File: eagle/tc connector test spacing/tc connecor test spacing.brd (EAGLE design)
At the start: 100 x 52 mm, 31 parts

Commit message: Inside and outside draft versions chosen.
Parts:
- removed U$1, U$10, U$11, U$12, U$15, U$16, U$17, U$18, U$19, U$2, U$20, U$21, U$22, U$23, U$24, U$27, U$28, U$3, U$4, U$5, U$6, U$7, U$8, U$9: TC-MINI-SINGLE, PaxInstruments-Connectors:TC-CLIP-SINGLE
- removed U$29, U$30: POGO-2.54-2P, PaxInstruments-Connectors:POGO-2.54-2P
- removed U$31: POGO-2.54-6P, PaxInstruments-Connectors:POGO-2.54-6P
- moved U$25 43.9 mm to (12.0, 44.0)
- moved U$26 43.9 mm to (5.00, 44.0)
- moved U$13 37.0 mm to (5.00, 6.00)
- moved U$14 37.0 mm to (15.0, 6.00)
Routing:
- net N$1: track 27.0 -> 0.00 mm
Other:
- board size 100 x 52 mm -> 50 x 52 mm
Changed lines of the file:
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@@
 <board>
 <plain>
-<wire x1="0" y1="0" x2="100" y2="0" width="0.1" layer="20"/>
-<wire x1="100" y1="0" x2="100" y2="52" width="0.1" layer="20"/>
-<wire x1="100" y1="52" x2="0" y2="52" width="0.1" layer="20"/>
+<wire x1="0" y1="0" x2="50" y2="0" width="0.1" layer="20"/>
+<wire x1="50" y1="0" x2="50" y2="52" width="0.1" layer="20"/>
+<wire x1="50" y1="52" x2="0" y2="52" width="0.1" layer="20"/>
 <wire x1="0" y1="52" x2="0" y2="0" width="0.1" layer="20"/>
 <dimension x1="2" y1="-4" x2="13" y2="-4" x3="7.5" y3="-7" textsize="1.778" layer="48"/>
 <dimension x1="17" y1="-4" x2="22" y2="-4" x3="19.5" y3="-7" textsize="1.778" layer="48"/>
-<wire x1="3.5" y1="38" x2="14.5" y2="38" width="0.4064" layer="48"/>
 <wire x1="17" y1="-3" x2="22" y2="-3" width="0.4064" layer="48"/>
-<wire x1="22" y1="38" x2="33" y2="38" width="0.4064" layer="48"/>
-<wire x1="41.5" y1="38" x2="52.5" y2="38" width="0.4064" layer="48"/>
-<wire x1="62" y1="38" x2="73" y2="38" width="0.4064" layer="48"/>
-<wire x1="83.5" y1="38" x2="94.5" y2="38" width="0.4064" layer="48"/>
 <wire x1="2" y1="-3" x2="13" y2="-3" width="0.4064" layer="48"/>
-<wire x1="6.5" y1="14" x2="11.5" y2="14" width="0.4064" layer="48"/>
-<wire x1="25" y1="14" x2="30" y2="14" width="0.4064" layer="48"/>
-<wire x1="44.5" y1="14" x2="49.5" y2="14" width="0.4064" layer="48"/>
-<wire x1="65" y1="14" x2="70" y2="14" width="0.4064" layer="48"/>
-<wire x1="86.5" y1="14" x2="91.5" y2="14" width="0.4064" layer="48"/>
-<wire x1="31" y1="18" x2="26" y2="18" width="0.4064" layer="48"/>
-<wire x1="11" y1="18" x2="6" y2="18" width="0.4064" layer="48"/>
-<wire x1="43.5" y1="18" x2="54.5" y2="18" width="0.4064" layer="48"/>
-<wire x1="63" y1="18" x2="74" y2="18" width="0.4064" layer="48"/>
-<wire x1="2" y1="31" x2="16" y2="31" width="0.8" layer="46"/>
-<wire x1="18" y1="31" x2="39" y2="31" width="0.8" layer="46"/>
-<wire x1="41" y1="31" x2="56" y2="31" width="0.8" layer="46"/>
-<wire x1="58" y1="31" x2="79" y2="31" width="0.8" layer="46"/>
-<wire x1="81" y1="31" x2="98" y2="31" width="0.8" layer="46"/>
+<wire x1="7.5" y1="14" x2="12.5" y2="14" width="0.4064" layer="48"/>
+<wire x1="3.5" y1="36" x2="14.5" y2="36" width="0.4064" layer="48"/>
 <dimension x1="26" y1="-4" x2="43" y2="-4" x3="34.5" y3="-7" textsize="1.778" layer="48"/>
 <wire x1="26" y1="-3" x2="43" y2="-3" width="0.4064" layer="48"/>
@@
 </autorouter>
 <elements>
-<element name="U$1" library="PaxInstruments-Connectors" package="TC-CLIP-SINGLE" value="TC-MINI-SINGLE" x="23" y="46"/>
-<element name="U$2" library="PaxInstruments-Connectors" package="TC-CLIP-SINGLE" value="TC-MINI-SINGLE" x="32" y="46" rot="R180"/>
-<element name="U$3" library="PaxInstruments-Connectors" package="TC-CLIP-SINGLE" value="TC-MINI-SINGLE" x="13" y="46" rot="R180"/>
-<element name="U$4" library="PaxInstruments-Connectors" package="TC-CLIP-SINGLE" value="TC-MINI-SINGLE" x="5" y="46"/>
-<element name="U$5" library="PaxInstruments-Connectors" package="TC-CLIP-SINGLE" value="TC-MINI-SINGLE" x="42" y="46"/>
-<element name="U$6" library="PaxInstruments-Connectors" package="TC-CLIP-SINGLE" value="TC-MINI-SINGLE" x="52" y="46" rot="R180"/>
-<element name="U$7" library="PaxInstruments-Connectors" package="TC-CLIP-SINGLE" value="TC-MINI-SINGLE" x="62" y="46"/>
-<element name="U$8" library="PaxInstruments-Connectors" package="TC-CLIP-SINGLE" value="TC-MINI-SINGLE" x="73" y="46" rot="R180"/>
-<element name="U$9" library="PaxInstruments-Connectors" package="TC-CLIP-SINGLE" value="TC-MINI-SINGLE" x="5" y="6" rot="R180"/>
-<element name="U$10" library="PaxInstruments-Connectors" package="TC-CLIP-SINGLE" value="TC-MINI-SINGLE" x="13" y="6"/>
-<element name="U$11" library="PaxInstruments-Connectors" package="TC-CLIP-SINGLE" value="TC-MINI-SINGLE" x="23" y="6" rot="R180"/>
-<element name="U$12" library="PaxInstruments-Connectors" package="TC-CLIP-SINGLE" value="TC-MINI-SINGLE" x="32" y="6"/>
-<element name="U$13" library="PaxInstruments-Connectors" package="TC-CLIP-SINGLE" value="TC-MINI-SINGLE" x="42" y="6" rot="R180"/>
-<element name="U$14" library="PaxInstruments-Connectors" package="TC-CLIP-SINGLE" value="TC-MINI-SINGLE" x="52" y="6"/>
-<element name="U$15" library="PaxInstruments-Connectors" package="TC-CLIP-SINGLE" value="TC-MINI-SINGLE" x="73" y="6"/>
-<element name="U$16" library="PaxInstruments-Connectors" package="TC-CLIP-SINGLE" value="TC-MINI-SINGLE" x="95" y="46" rot="R180"/>
-<element name="U$17" library="PaxInstruments-Connectors" package="TC-CLIP-SINGLE" value="TC-MINI-SINGLE" x="62" y="6" rot="R180"/>
-<element name="U$18" library="PaxInstruments-Connectors" package="TC-CLIP-SINGLE" value="TC-MINI-SINGLE" x="83" y="46"/>
-<element name="U$19" library="PaxInstruments-Connectors" package="TC-CLIP-SINGLE" value="TC-MINI-SINGLE" x="22" y="26" rot="R180"/>
-<element name="U$20" library="PaxInstruments-Connectors" package="TC-CLIP-SINGLE" value="TC-MINI-SINGLE" x="12" y="26"/>
-<element name="U$21" library="PaxInstruments-Connectors" package="TC-CLIP-SINGLE" value="TC-MINI-SINGLE" x="83" y="6" rot="R180"/>
-<element name="U$22" library="PaxInstruments-Connectors" package="TC-CLIP-SINGLE" value="TC-MINI-SINGLE" x="95" y="6"/>
-<element name="U$23" library="PaxInstruments-Connectors" package="TC-CLIP-SINGLE" value="TC-MINI-SINGLE" x="35" y="26"/>
-<element name="U$24" library="PaxInstruments-Connectors" package="TC-CLIP-SINGLE" value="TC-MINI-SINGLE" x="5" y="26" rot="R180"/>
-<element name="U$25" library="PaxInstruments-Connectors" package="TC-CLIP-SINGLE" value="TC-MINI-SINGLE" x="52" y="26" rot="R180"/>
-<element name="U$26" library="PaxInstruments-Connectors" package="TC-CLIP-SINGLE" value="TC-MINI-SINGLE" x="45" y="26"/>
-<element name="U$27" library="PaxInstruments-Connectors" package="TC-CLIP-SINGLE" value="TC-MINI-SINGLE" x="62" y="26"/>
-<element name="U$28" library="PaxInstruments-Connectors" package="TC-CLIP-SINGLE" value="TC-MINI-SINGLE" x="75" y="26" rot="R180"/>
-<element name="U$29" library="PaxInstruments-Connectors" package="POGO-2.54-2P" value="POGO-2.54-2P" x="83" y="28"/>
-<element name="U$30" library="PaxInstruments-Connectors" package="POGO-2.54-2P" value="POGO-2.54-2P" x="93" y="28"/>
-<element name="U$31" library="PaxInstruments-Connectors" package="POGO-2.54-6P" value="POGO-2.54-6P" x="83" y="21"/>
+<element name="U$13" library="PaxInstruments-Connectors" package="TC-CLIP-SINGLE" value="TC-MINI-SINGLE" x="5" y="6" rot="R180"/>
+<element name="U$14" library="PaxInstruments-Connectors" package="TC-CLIP-SINGLE" value="TC-MINI-SINGLE" x="15" y="6"/>
+<element name="U$25" library="PaxInstruments-Connectors" package="TC-CLIP-SINGLE" value="TC-MINI-SINGLE" x="12" y="44" rot="R180"/>
+<element name="U$26" library="PaxInstruments-Connectors" package="TC-CLIP-SINGLE" value="TC-MINI-SINGLE" x="5" y="44"/>
 </elements>
 <signals>
-<signal name="N$1">
-<wire x1="15" y1="14" x2="40" y2="14" width="0.4064" layer="16"/>
-<wire x1="40" y1="14" x2="40" y2="16" width="0.4064" layer="16"/>
-</signal>
 </signals>
 </board>

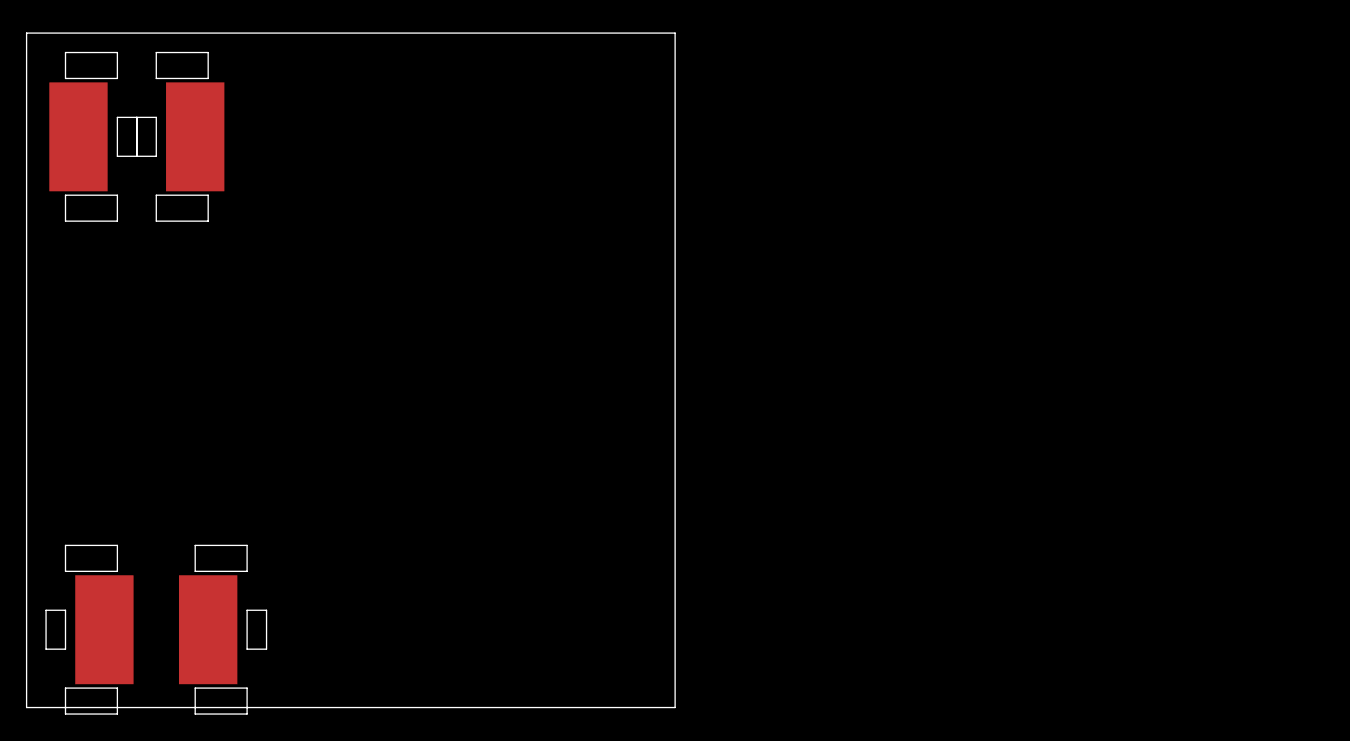
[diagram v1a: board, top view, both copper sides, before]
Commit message: This could be the production footprint.:
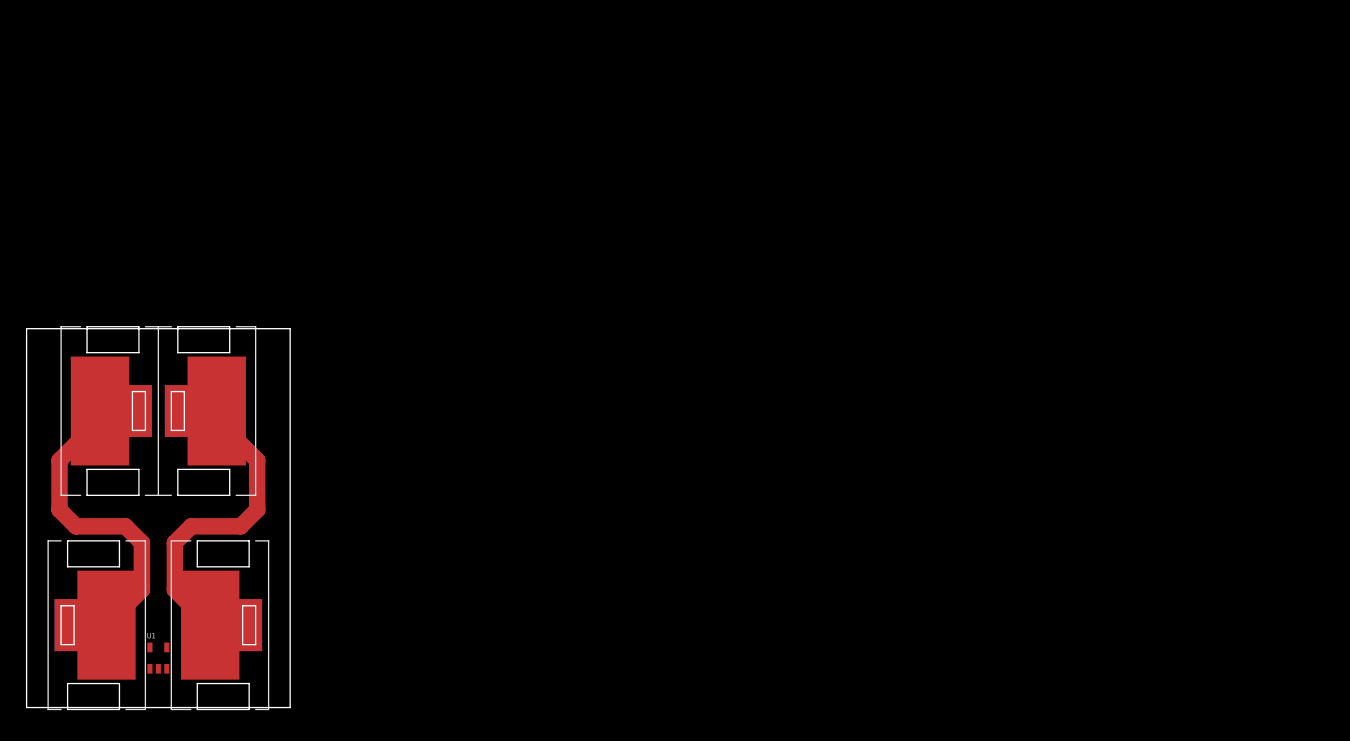
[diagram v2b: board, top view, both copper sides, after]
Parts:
- removed U$13, U$14, U$25, U$26: TC-MINI-SINGLE, PaxInstruments-Connectors:TC-CLIP-SINGLE
- added U$1: TC-MINI-INSIDE, PaxInstruments-Connectors:TC-CLIP-INSIDE
- added U$2: TC-MINI-OUTSIDE, PaxInstruments-Connectors:TC-CLIP-OUTSIDE
- added U1: NC7SPU04, SparkFun-DigitalIC:SC70
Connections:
- new net N$1: U$1.P$1, U$2.P$2
- new net N$2: U$1.P$2, U$2.P$1
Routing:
- net N$2: track 0.00 -> 23.8 mm
- net N$1: track 0.00 -> 23.8 mm
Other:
- board size 50 x 52 mm -> 20.3 x 29.2 mm
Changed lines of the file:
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@@
 <setting verticaltext="up"/>
 </settings>
-<grid distance="1" unitdist="mm" unit="mm" style="lines" multiple="1" display="yes" altdistance="0.025" altunitdist="inch" altunit="inch"/>
+<grid distance="0.05" unitdist="inch" unit="inch" style="lines" multiple="1" display="yes" altdistance="0.025" altunitdist="inch" altunit="inch"/>
 <layers>
 <layer number="1" name="Top" color="4" fill="1" visible="yes" active="yes"/>
@@
 <layer number="54" name="bGND_GNDA" color="7" fill="1" visible="no" active="no"/>
 <layer number="56" name="wert" color="7" fill="1" visible="no" active="no"/>
+<layer number="57" name="tCAD" color="7" fill="1" visible="no" active="no"/>
+<layer number="59" name="tCarbon" color="7" fill="1" visible="no" active="no"/>
+<layer number="60" name="bCarbon" color="7" fill="1" visible="no" active="no"/>
+<layer number="90" name="Modules" color="5" fill="1" visible="yes" active="yes"/>
 <layer number="91" name="Nets" color="2" fill="1" visible="no" active="no"/>
 <layer number="92" name="Busses" color="1" fill="1" visible="no" active="no"/>
@@
 <layer number="127" name="_tValues" color="7" fill="1" visible="yes" active="yes"/>
 <layer number="128" name="_bValues" color="7" fill="1" visible="yes" active="yes"/>
+<layer number="129" name="Mask" color="7" fill="1" visible="yes" active="yes"/>
 <layer number="131" name="tAdjust" color="7" fill="1" visible="yes" active="yes"/>
 <layer number="132" name="bAdjust" color="7" fill="1" visible="yes" active="yes"/>
 <layer number="144" name="Drill_legend" color="7" fill="1" visible="yes" active="yes"/>
+<layer number="150" name="Notes" color="7" fill="1" visible="yes" active="yes"/>
 <layer number="151" name="HeatSink" color="7" fill="1" visible="yes" active="yes"/>
 <layer number="152" name="_bDocu" color="7" fill="1" visible="yes" active="yes"/>
+<layer number="153" name="FabDoc1" color="7" fill="1" visible="yes" active="yes"/>
+<layer number="154" name="FabDoc2" color="7" fill="1" visible="yes" active="yes"/>
+<layer number="155" name="FabDoc3" color="7" fill="1" visible="yes" active="yes"/>
 <layer number="199" name="Contour" color="7" fill="1" visible="yes" active="yes"/>
 <layer number="200" name="200bmp" color="7" fill="1" visible="yes" active="yes"/>
@@
 <layer number="223" name="223bmp" color="7" fill="1" visible="yes" active="yes"/>
 <layer number="224" name="224bmp" color="7" fill="1" visible="yes" active="yes"/>
+<layer number="225" name="225bmp" color="7" fill="1" visible="yes" active="yes"/>
+<layer number="226" name="226bmp" color="7" fill="1" visible="yes" active="yes"/>
+<layer number="227" name="227bmp" color="7" fill="1" visible="yes" active="yes"/>
+<layer number="228" name="228bmp" color="7" fill="1" visible="yes" active="yes"/>
+<layer number="229" name="229bmp" color="7" fill="1" visible="yes" active="yes"/>
+<layer number="230" name="230bmp" color="7" fill="1" visible="yes" active="yes"/>
 <layer number="231" name="Eagle3D_PG1" color="7" fill="1" visible="yes" active="yes"/>
 <layer number="232" name="Eagle3D_PG2" color="7" fill="1" visible="yes" active="yes"/>
@@
 <layer number="251" name="SMDround" color="7" fill="1" visible="yes" active="yes"/>
 <layer number="254" name="cooling" color="7" fill="1" visible="yes" active="yes"/>
+<layer number="255" name="routoute" color="7" fill="1" visible="yes" active="yes"/>
 </layers>
 <board>
 <plain>
-<wire x1="0" y1="0" x2="50" y2="0" width="0.1" layer="20"/>
-<wire x1="50" y1="0" x2="50" y2="52" width="0.1" layer="20"/>
-<wire x1="50" y1="52" x2="0" y2="52" width="0.1" layer="20"/>
-<wire x1="0" y1="52" x2="0" y2="0" width="0.1" layer="20"/>
-<dimension x1="2" y1="-4" x2="13" y2="-4" x3="7.5" y3="-7" textsize="1.778" layer="48"/>
-<dimension x1="17" y1="-4" x2="22" y2="-4" x3="19.5" y3="-7" textsize="1.778" layer="48"/>
-<wire x1="17" y1="-3" x2="22" y2="-3" width="0.4064" layer="48"/>
-<wire x1="2" y1="-3" x2="13" y2="-3" width="0.4064" layer="48"/>
-<wire x1="7.5" y1="14" x2="12.5" y2="14" width="0.4064" layer="48"/>
-<wire x1="3.5" y1="36" x2="14.5" y2="36" width="0.4064" layer="48"/>
-<dimension x1="26" y1="-4" x2="43" y2="-4" x3="34.5" y3="-7" textsize="1.778" layer="48"/>
-<wire x1="26" y1="-3" x2="43" y2="-3" width="0.4064" layer="48"/>
+<wire x1="0" y1="0" x2="20.32" y2="0" width="0.1" layer="20"/>
+<wire x1="20.32" y1="0" x2="20.32" y2="29.21" width="0.1" layer="20"/>
+<wire x1="20.32" y1="29.21" x2="0" y2="29.21" width="0.1" layer="20"/>
+<wire x1="0" y1="29.21" x2="0" y2="0" width="0.1" layer="20"/>
 </plain>
 <attributes>
@@
 </autorouter>
 <elements>
-<element name="U$13" library="PaxInstruments-Connectors" package="TC-CLIP-SINGLE" value="TC-MINI-SINGLE" x="5" y="6" rot="R180"/>
-<element name="U$14" library="PaxInstruments-Connectors" package="TC-CLIP-SINGLE" value="TC-MINI-SINGLE" x="15" y="6"/>
-<element name="U$25" library="PaxInstruments-Connectors" package="TC-CLIP-SINGLE" value="TC-MINI-SINGLE" x="12" y="44" rot="R180"/>
-<element name="U$26" library="PaxInstruments-Connectors" package="TC-CLIP-SINGLE" value="TC-MINI-SINGLE" x="5" y="44"/>
+<element name="U$1" library="PaxInstruments-Connectors" package="TC-CLIP-INSIDE" value="TC-MINI-INSIDE" x="10.16" y="6.35"/>
+<element name="U$2" library="PaxInstruments-Connectors" package="TC-CLIP-OUTSIDE" value="TC-MINI-OUTSIDE" x="10.16" y="22.86"/>
+<element name="U1" library="SparkFun-DigitalIC" package="SC70" value="NC7SPU04" x="10.16" y="3.81">
+<attribute name="PROD_ID" value="8803" x="10.16" y="3.81" size="1.778" layer="27" display="off"/>
+</element>
 </elements>
 <signals>
+<signal name="N$1">
+<contactref element="U$1" pad="P$1"/>
+<contactref element="U$2" pad="P$2"/>
+<wire x1="6.16" y1="6.35" x2="8.89" y2="9.08" width="1.27" layer="1"/>
+<wire x1="8.89" y1="9.08" x2="8.89" y2="12.7" width="1.27" layer="1"/>
+<wire x1="8.89" y1="12.7" x2="7.62" y2="13.97" width="1.27" layer="1"/>
+<wire x1="7.62" y1="13.97" x2="3.81" y2="13.97" width="1.27" layer="1"/>
+<wire x1="3.81" y1="13.97" x2="2.54" y2="15.24" width="1.27" layer="1"/>
+<wire x1="2.54" y1="15.24" x2="2.54" y2="19.05" width="1.27" layer="1"/>
+<wire x1="2.54" y1="19.05" x2="5.66" y2="22.17" width="1.27" layer="1"/>
+<wire x1="5.66" y1="22.17" x2="5.66" y2="22.86" width="1.27" layer="1"/>
+</signal>
+<signal name="N$2">
+<contactref element="U$1" pad="P$2"/>
+<contactref element="U$2" pad="P$1"/>
+<wire x1="14.16" y1="6.35" x2="11.43" y2="9.08" width="1.27" layer="1"/>
+<wire x1="11.43" y1="9.08" x2="11.43" y2="12.7" width="1.27" layer="1"/>
+<wire x1="11.43" y1="12.7" x2="12.7" y2="13.97" width="1.27" layer="1"/>
+<wire x1="12.7" y1="13.97" x2="16.51" y2="13.97" width="1.27" layer="1"/>
+<wire x1="16.51" y1="13.97" x2="17.78" y2="15.24" width="1.27" layer="1"/>
+<wire x1="17.78" y1="15.24" x2="17.78" y2="19.05" width="1.27" layer="1"/>
+<wire x1="17.78" y1="19.05" x2="14.66" y2="22.17" width="1.27" layer="1"/>
+<wire x1="14.66" y1="22.17" x2="14.66" y2="22.86" width="1.27" layer="1"/>
+</signal>
 </signals>
 </board>
